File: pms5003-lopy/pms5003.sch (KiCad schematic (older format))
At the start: 23 parts, among them J1 Battery, J2 DS3231, J3 PMS5003, J4 SHT10, J5 P2, J6 PROG, J7 USB_OTG, Q1 IRF540N, Q2 IRF7309IPBF, U1 U3V12F5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

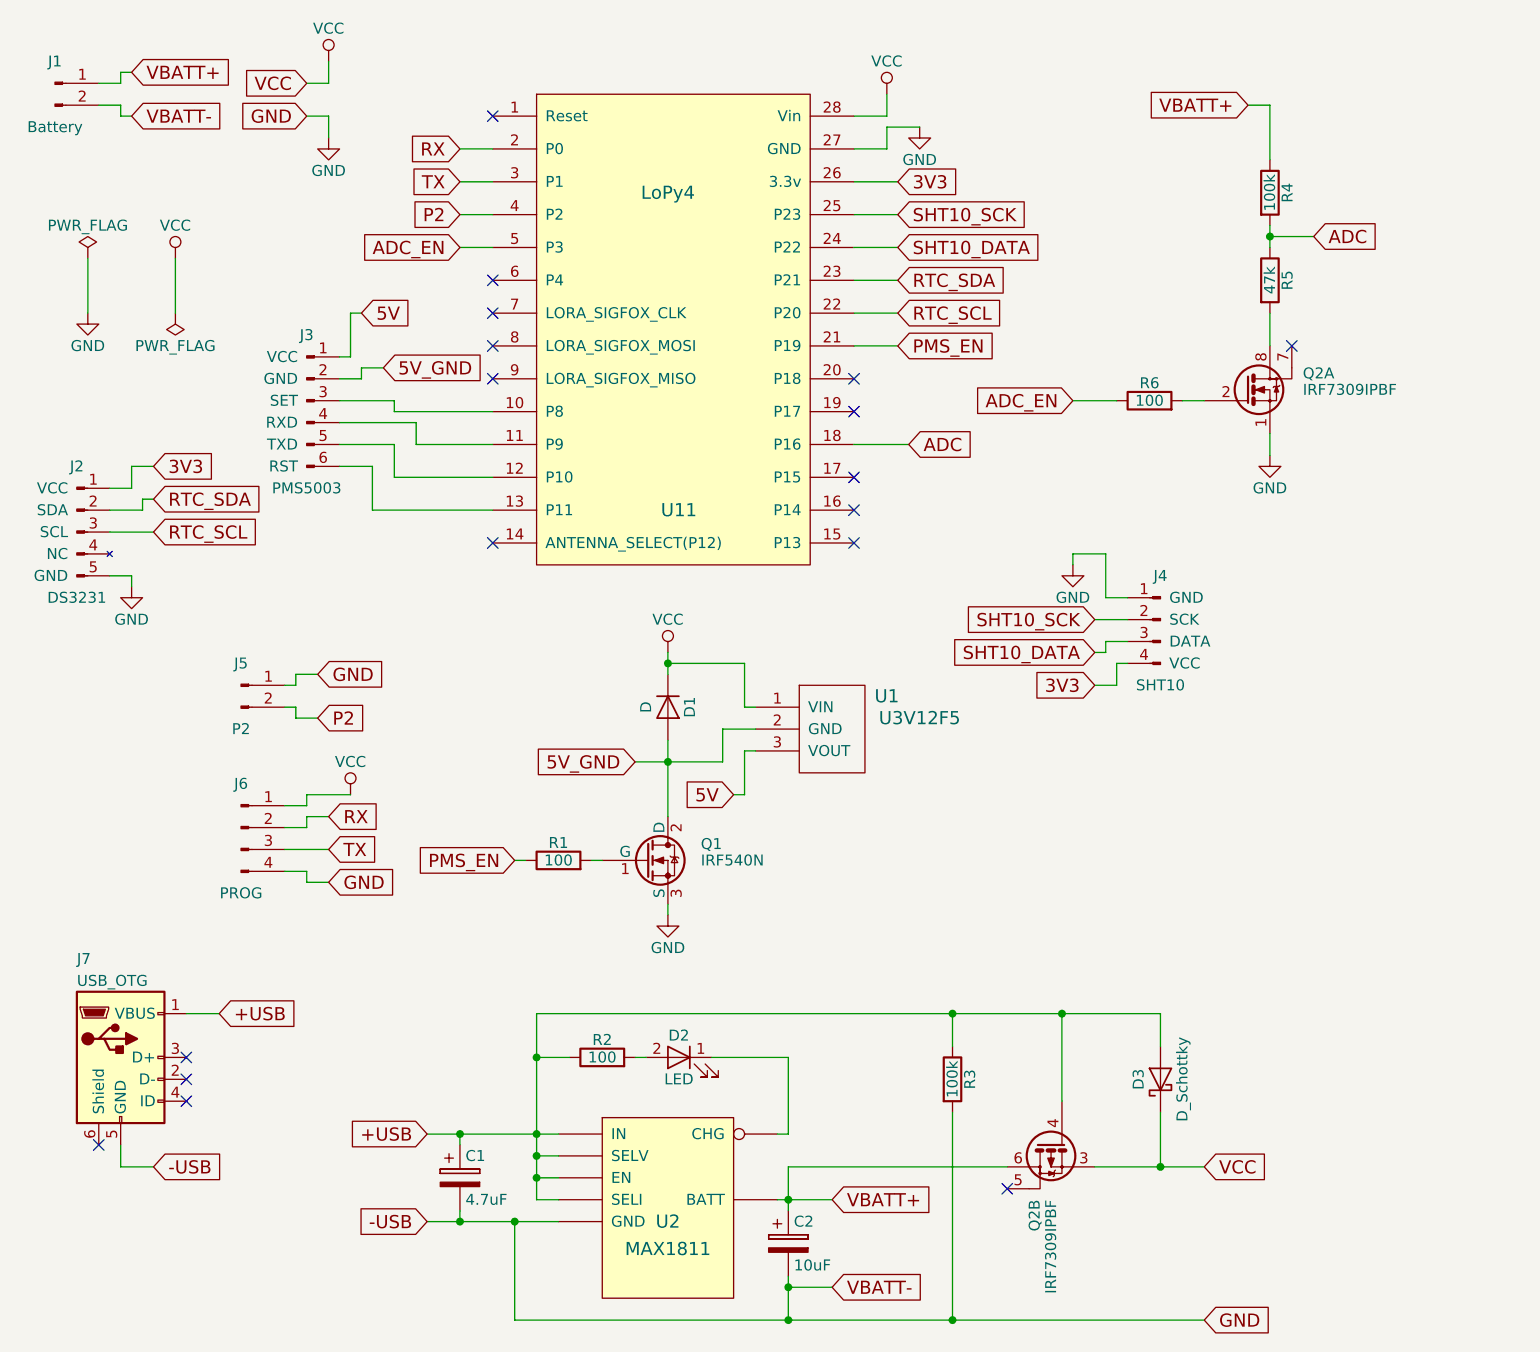
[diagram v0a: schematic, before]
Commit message: PMS5003-lopy: Add VCC pin for SHT10/RTC
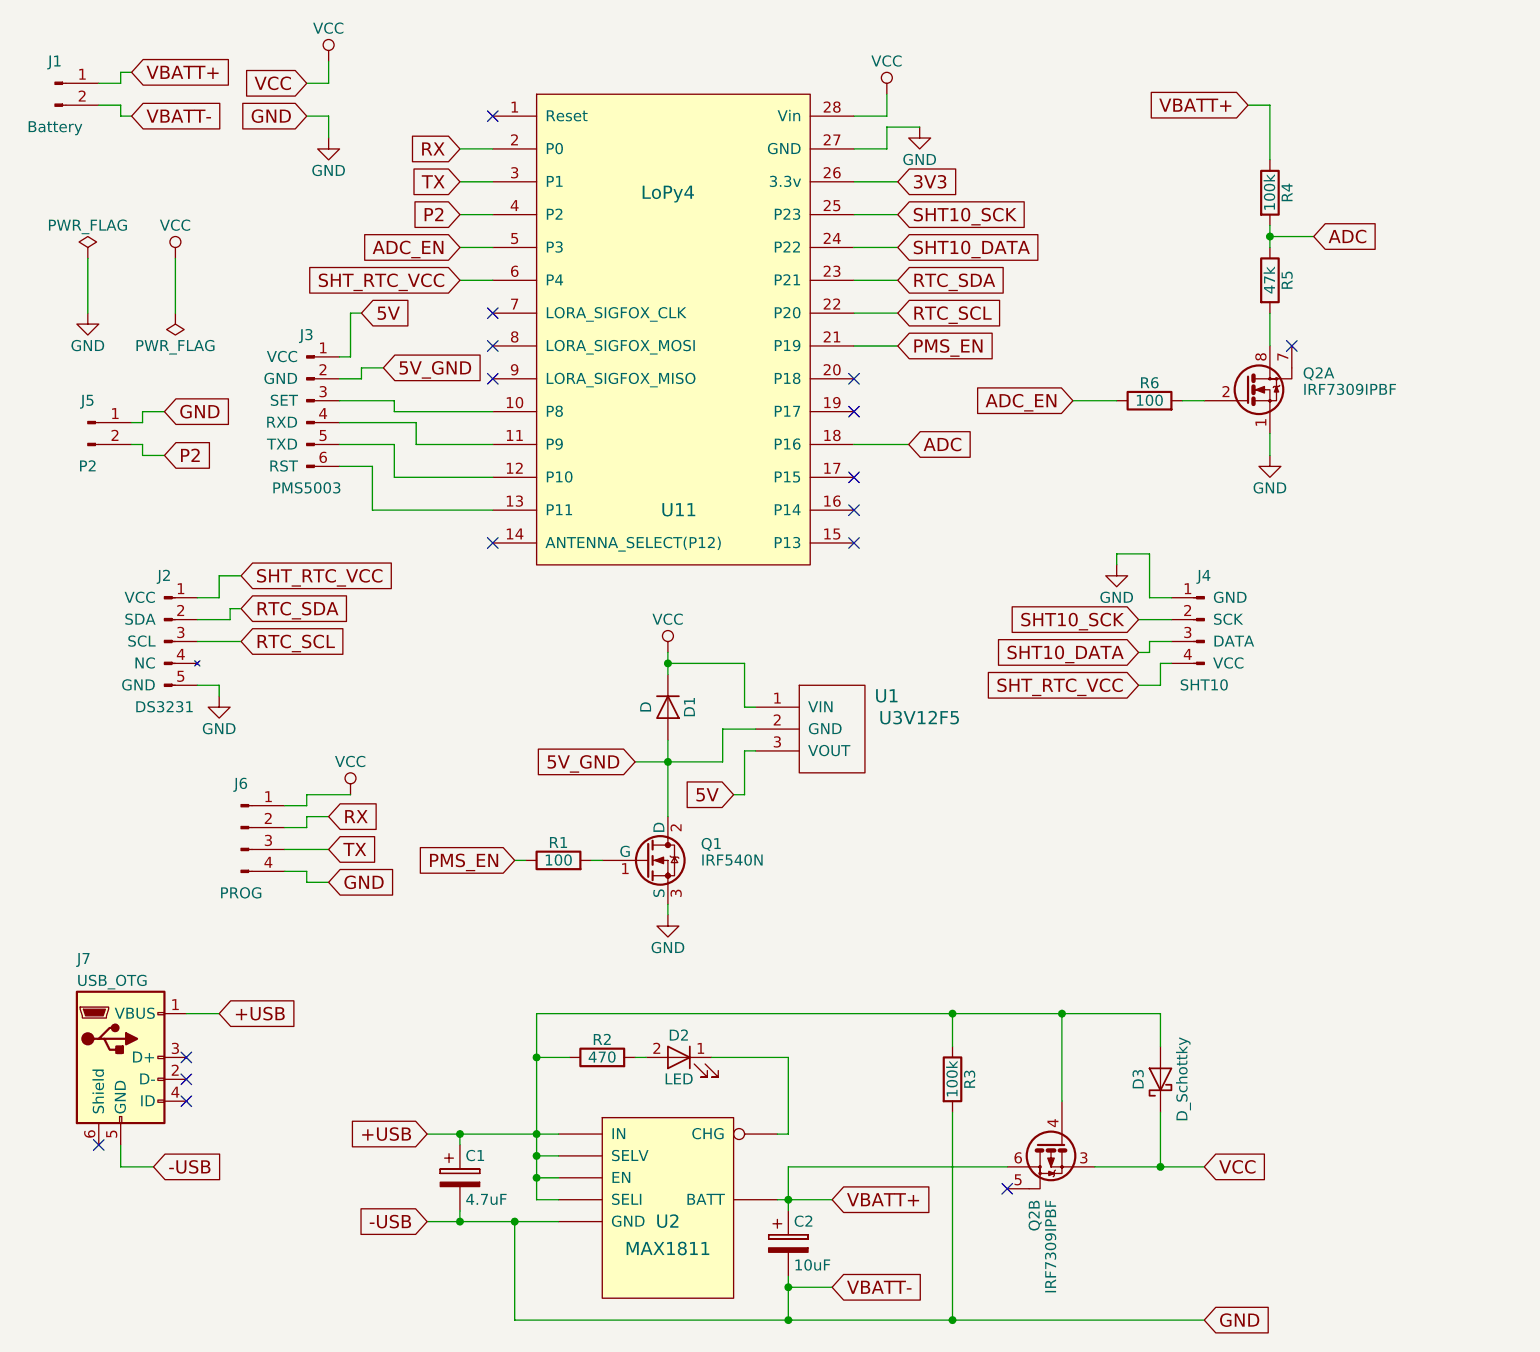
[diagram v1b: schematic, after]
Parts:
- R2: value 100 -> 470
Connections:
- net 3V3: no longer J2.1 (VCC), J4.4 (VCC)
- net SHT_RTC_VCC: now reaches U11.6 (P4)
- net SHT_RTC_VCC: now also J2.1 (VCC), J4.4 (VCC)
- no-connect marks 17 -> 16
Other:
- moved on the sheet: J2, J4, J5
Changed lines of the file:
@@
 L SHT10 J4
 U 1 1 5A61FF89
-P 5700 3350
-F 0 "J4" H 5700 3550 50  0000 C CNN
-F 1 "SHT10" H 5700 3050 50  0000 C CNN
-F 2 "Socket_Strips:Socket_Strip_Angled_1x04_Pitch2.54mm" H 5700 3350 50  0001 C CNN
-F 3 "" H 5700 3350 50  0001 C CNN
-	1    5700 3350
+P 5900 3350
+F 0 "J4" H 5900 3550 50  0000 C CNN
+F 1 "SHT10" H 5900 3050 50  0000 C CNN
+F 2 "Socket_Strips:Socket_Strip_Angled_1x04_Pitch2.54mm" H 5900 3350 50  0001 C CNN
+F 3 "" H 5900 3350 50  0001 C CNN
+	1    5900 3350
 	-1   0    0    -1
 $EndComp
@@
 L DS3231 J2
 U 1 1 5A620243
-P 750 2950
-F 0 "J2" H 750 3250 50  0000 C CNN
-F 1 "DS3231" H 750 2650 50  0000 C CNN
-F 2 "Socket_Strips:Socket_Strip_Straight_1x05_Pitch2.54mm" H 750 2950 50  0001 C CNN
-F 3 "" H 750 2950 50  0001 C CNN
-	1    750  2950
+P 1150 3450
+F 0 "J2" H 1150 3750 50  0000 C CNN
+F 1 "DS3231" H 1150 3150 50  0000 C CNN
+F 2 "Socket_Strips:Socket_Strip_Straight_1x05_Pitch2.54mm" H 1150 3450 50  0001 C CNN
+F 3 "" H 1150 3450 50  0001 C CNN
+	1    1150 3450
 	1    0    0    -1
 $EndComp
@@
 Text GLabel 4500 1350 2    60   Input ~ 0
 3V3
-Text GLabel 5400 3650 0    60   Input ~ 0
-3V3
+Text GLabel 5600 3650 0    60   Input ~ 0
+SHT_RTC_VCC
 $Comp
 L GND #PWR03
 U 1 1 5A6216BF
-P 5300 3100
-F 0 "#PWR03" H 5300 2850 50  0001 C CNN
-F 1 "GND" H 5300 2950 50  0000 C CNN
-F 2 "" H 5300 3100 50  0001 C CNN
-F 3 "" H 5300 3100 50  0001 C CNN
-	1    5300 3100
+P 5500 3100
+F 0 "#PWR03" H 5500 2850 50  0001 C CNN
+F 1 "GND" H 5500 2950 50  0000 C CNN
+F 2 "" H 5500 3100 50  0001 C CNN
+F 3 "" H 5500 3100 50  0001 C CNN
+	1    5500 3100
 	1    0    0    -1
 $EndComp
@@
 	4500 1350 4300 1350
 Wire Wire Line
-	5550 3550 5500 3550
-Wire Wire Line
-	5300 3100 5300 3050
-Wire Wire Line
-	5300 3050 5450 3050
-Wire Wire Line
-	5450 3050 5450 3250
-Wire Wire Line
-	5450 3250 5550 3250
+	5750 3550 5700 3550
+Wire Wire Line
+	5500 3100 5500 3050
+Wire Wire Line
+	5500 3050 5650 3050
+Wire Wire Line
+	5650 3050 5650 3250
+Wire Wire Line
+	5650 3250 5750 3250
 Wire Wire Line
 	1900 1150 1900 1050
@@
 Wire Wire Line
 	4450 1050 4450 950
-Text GLabel 1100 2650 2    60   Input ~ 0
-3V3
-Wire Wire Line
-	1100 2650 1000 2650
-Wire Wire Line
-	1000 2650 1000 2750
-Wire Wire Line
-	1000 2750 900  2750
+Text GLabel 1500 3150 2    60   Input ~ 0
+SHT_RTC_VCC
+Wire Wire Line
+	1500 3150 1400 3150
+Wire Wire Line
+	1400 3150 1400 3250
+Wire Wire Line
+	1400 3250 1300 3250
 $Comp
 L GND #PWR08
 U 1 1 5A621BA2
-P 1000 3200
-F 0 "#PWR08" H 1000 2950 50  0001 C CNN
-F 1 "GND" H 1000 3050 50  0000 C CNN
-F 2 "" H 1000 3200 50  0001 C CNN
-F 3 "" H 1000 3200 50  0001 C CNN
-	1    1000 3200
-	1    0    0    -1
-$EndComp
-Wire Wire Line
-	1000 3200 1000 3150
-Wire Wire Line
-	1000 3150 900  3150
-Text GLabel 5400 3350 0    60   Input ~ 0
+P 1400 3700
+F 0 "#PWR08" H 1400 3450 50  0001 C CNN
+F 1 "GND" H 1400 3550 50  0000 C CNN
+F 2 "" H 1400 3700 50  0001 C CNN
+F 3 "" H 1400 3700 50  0001 C CNN
+	1    1400 3700
+	1    0    0    -1
+$EndComp
+Wire Wire Line
+	1400 3700 1400 3650
+Wire Wire Line
+	1400 3650 1300 3650
+Text GLabel 5600 3350 0    60   Input ~ 0
 SHT10_SCK
 Wire Wire Line
-	5500 3550 5500 3650
-Wire Wire Line
-	5500 3650 5400 3650
-Wire Wire Line
-	5400 3350 5550 3350
-Text GLabel 5400 3500 0    60   Input ~ 0
+	5700 3550 5700 3650
+Wire Wire Line
+	5700 3650 5600 3650
+Wire Wire Line
+	5600 3350 5750 3350
+Text GLabel 5600 3500 0    60   Input ~ 0
 SHT10_DATA
 Wire Wire Line
-	5400 3500 5450 3500
-Wire Wire Line
-	5450 3500 5450 3450
-Wire Wire Line
-	5450 3450 5550 3450
+	5600 3500 5650 3500
+Wire Wire Line
+	5650 3500 5650 3450
+Wire Wire Line
+	5650 3450 5750 3450
 Text GLabel 4500 1500 2    60   Input ~ 0
 SHT10_SCK
@@
 Wire Wire Line
 	4500 1650 4300 1650
-Text GLabel 1100 2800 2    60   Input ~ 0
+Text GLabel 1500 3300 2    60   Input ~ 0
 RTC_SDA
-Text GLabel 1100 2950 2    60   Input ~ 0
+Text GLabel 1500 3450 2    60   Input ~ 0
 RTC_SCL
 Wire Wire Line
-	900  2850 1050 2850
-Wire Wire Line
-	1050 2850 1050 2800
-Wire Wire Line
-	1050 2800 1100 2800
-Wire Wire Line
-	1100 2950 900  2950
+	1300 3350 1450 3350
+Wire Wire Line
+	1450 3350 1450 3300
+Wire Wire Line
+	1450 3300 1500 3300
+Wire Wire Line
+	1500 3450 1300 3450
 Text GLabel 4500 1800 2    60   Input ~ 0
 RTC_SDA
@@
 L Conn_01x02_Male J5
 U 1 1 5A623BED
-P 1500 3650
-F 0 "J5" H 1500 3750 50  0000 C CNN
-F 1 "P2" H 1500 3450 50  0000 C CNN
-F 2 "Socket_Strips:Socket_Strip_Straight_1x02_Pitch2.54mm" H 1500 3650 50  0001 C CNN
-F 3 "" H 1500 3650 50  0001 C CNN
-	1    1500 3650
-	1    0    0    -1
-$EndComp
-Text GLabel 1850 3800 2    60   Input ~ 0
+P 800 2450
+F 0 "J5" H 800 2550 50  0000 C CNN
+F 1 "P2" H 800 2250 50  0000 C CNN
+F 2 "Socket_Strips:Socket_Strip_Straight_1x02_Pitch2.54mm" H 800 2450 50  0001 C CNN
+F 3 "" H 800 2450 50  0001 C CNN
+	1    800  2450
+	1    0    0    -1
+$EndComp
+Text GLabel 1150 2600 2    60   Input ~ 0
 P2
-Text GLabel 1850 3600 2    60   Input ~ 0
+Text GLabel 1150 2400 2    60   Input ~ 0
 GND
 Wire Wire Line
-	1700 3650 1750 3650
-Wire Wire Line
-	1750 3650 1750 3600
-Wire Wire Line
-	1750 3600 1850 3600
-Wire Wire Line
-	1700 3750 1750 3750
-Wire Wire Line
-	1750 3750 1750 3800
-Wire Wire Line
-	1750 3800 1850 3800
+	1000 2450 1050 2450
+Wire Wire Line
+	1050 2450 1050 2400
+Wire Wire Line
+	1050 2400 1150 2400
+Wire Wire Line
+	1000 2550 1050 2550
+Wire Wire Line
+	1050 2550 1050 2600
+Wire Wire Line
+	1050 2600 1150 2600
 Text GLabel 1900 4550 2    60   Input ~ 0
 GND
@@
 P 3150 5350
 F 0 "R2" V 3230 5350 50  0000 C CNN
-F 1 "100" V 3150 5350 50  0000 C CNN
+F 1 "470" V 3150 5350 50  0000 C CNN
 F 2 "Resistors_SMD:R_1206" V 3080 5350 50  0001 C CNN
 F 3 "" H 3150 5350 50  0001 C CNN
@@
 NoConn ~ 1250 5550
 NoConn ~ 850  5750
-NoConn ~ 2650 1800
 Text GLabel 6100 1000 0    60   Input ~ 0
 VBATT+
@@
 Wire Wire Line
 	5500 2350 5300 2350
+Text GLabel 2500 1800 0    60   Input ~ 0
+SHT_RTC_VCC
+Wire Wire Line
+	2650 1800 2500 1800
 $EndSCHEMATC

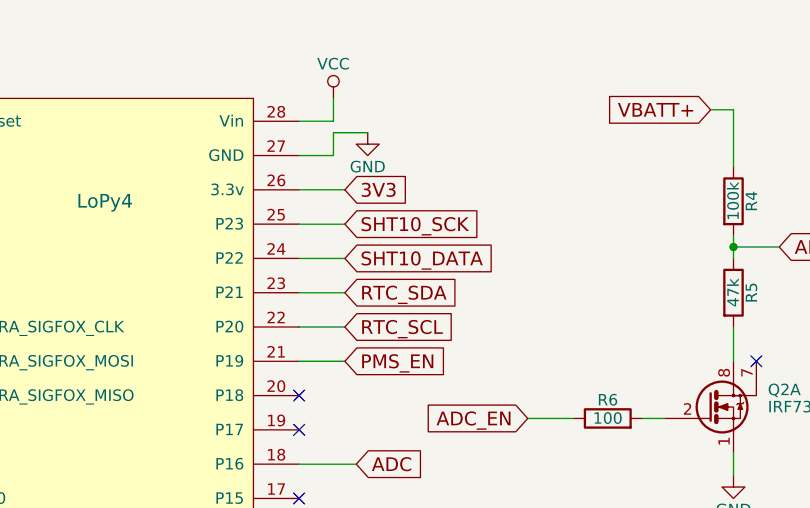
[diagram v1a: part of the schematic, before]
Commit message: PMS5003-lopy with AQ monitor on the board
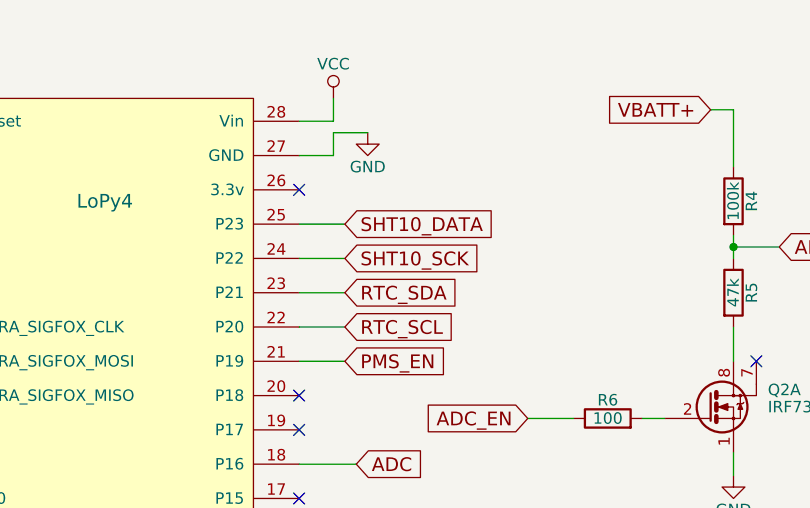
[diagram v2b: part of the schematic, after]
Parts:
- D3: footprint Diodes_SMD:D_SMA -> Diodes_SMD:D_SMB; 1st Distrib Link (none) -> Value; 1st Distrib PN (none) -> Value; 2nd Distrib Link (none) -> Value; 2nd Distrib PN (none) -> Value; MFG Name (none) -> Value; MFG Part Num (none) -> Value
- J2: footprint Socket_Strips:Socket_Strip_Straight_1x05_Pitch2.54mm -> various:DS3231; 1st Distrib Link (none) -> Value; 1st Distrib PN (none) -> Value; 2nd Distrib Link (none) -> Value; 2nd Distrib PN (none) -> Value; MFG Name (none) -> Value; MFG Part Num (none) -> Value
- J7: footprint Connectors:USB_Micro-B -> various:USB_Micro-B_91-US01-517; 1st Distrib Link (none) -> Value; 1st Distrib PN (none) -> Value; 2nd Distrib Link (none) -> Value; 2nd Distrib PN (none) -> Value; MFG Name (none) -> Value; MFG Part Num (none) -> Value
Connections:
- net SHT10_DATA: now also U11.25 (P23); no longer U11.24 (P22)
- net SHT10_SCK: now also U11.24 (P22); no longer U11.25 (P23)
- net 3V3: no longer names the net of U11.26 (3.3v)
- no-connect marks 16 -> 17
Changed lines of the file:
@@
 F 0 "J2" H 1150 3750 50  0000 C CNN
 F 1 "DS3231" H 1150 3150 50  0000 C CNN
-F 2 "Socket_Strips:Socket_Strip_Straight_1x05_Pitch2.54mm" H 1150 3450 50  0001 C CNN
+F 2 "various:DS3231" H 1150 3450 50  0001 C CNN
 F 3 "" H 1150 3450 50  0001 C CNN
+F 4 "Value" H 1150 3450 60  0001 C CNN "MFG Name"
+F 5 "Value" H 1150 3450 60  0001 C CNN "MFG Part Num"
+F 6 "Value" H 1150 3450 60  0001 C CNN "1st Distrib PN"
+F 7 "Value" H 1150 3450 60  0001 C CNN "1st Distrib Link"
+F 8 "Value" H 1150 3450 60  0001 C CNN "2nd Distrib PN"
+F 9 "Value" H 1150 3450 60  0001 C CNN "2nd Distrib Link"
 	1    1150 3450
 	1    0    0    -1
@@
 Text GLabel 2050 1950 2    60   Input ~ 0
 5V
-Text GLabel 4500 1350 2    60   Input ~ 0
-3V3
 Text GLabel 5600 3650 0    60   Input ~ 0
 SHT_RTC_VCC
@@
 	2000 1950 2050 1950
 Wire Wire Line
-	4500 1350 4300 1350
-Wire Wire Line
 	5750 3550 5700 3550
 Wire Wire Line
@@
 	5650 3450 5750 3450
 Text GLabel 4500 1500 2    60   Input ~ 0
+SHT10_DATA
+Text GLabel 4500 1650 2    60   Input ~ 0
 SHT10_SCK
-Text GLabel 4500 1650 2    60   Input ~ 0
-SHT10_DATA
 Wire Wire Line
 	4500 1500 4300 1500
@@
 F 0 "D3" H 5700 5550 50  0000 C CNN
 F 1 "D_Schottky" H 5700 5350 50  0000 C CNN
-F 2 "Diodes_SMD:D_SMA" H 5700 5450 50  0001 C CNN
+F 2 "Diodes_SMD:D_SMB" H 5700 5450 50  0001 C CNN
 F 3 "" H 5700 5450 50  0001 C CNN
+F 4 "Value" H 5700 5450 60  0001 C CNN "MFG Name"
+F 5 "Value" H 5700 5450 60  0001 C CNN "MFG Part Num"
+F 6 "Value" H 5700 5450 60  0001 C CNN "1st Distrib PN"
+F 7 "Value" H 5700 5450 60  0001 C CNN "1st Distrib Link"
+F 8 "Value" H 5700 5450 60  0001 C CNN "2nd Distrib PN"
+F 9 "Value" H 5700 5450 60  0001 C CNN "2nd Distrib Link"
 	1    5700 5450
 	0    -1   -1   0
@@
 F 0 "J7" H 750 5800 50  0000 L CNN
 F 1 "USB_OTG" H 750 5700 50  0000 L CNN
-F 2 "Connectors:USB_Micro-B" H 1100 5300 50  0001 C CNN
+F 2 "various:USB_Micro-B_91-US01-517" H 1100 5300 50  0001 C CNN
 F 3 "" H 1100 5300 50  0001 C CNN
+F 4 "Value" H 950 5350 60  0001 C CNN "MFG Name"
+F 5 "Value" H 950 5350 60  0001 C CNN "MFG Part Num"
+F 6 "Value" H 950 5350 60  0001 C CNN "1st Distrib PN"
+F 7 "Value" H 950 5350 60  0001 C CNN "1st Distrib Link"
+F 8 "Value" H 950 5350 60  0001 C CNN "2nd Distrib PN"
+F 9 "Value" H 950 5350 60  0001 C CNN "2nd Distrib Link"
 	1    950  5350
 	1    0    0    -1
@@
 Wire Wire Line
 	2650 1800 2500 1800
+NoConn ~ 4300 1350
 $EndSCHEMATC
